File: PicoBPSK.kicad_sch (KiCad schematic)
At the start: 0 parts

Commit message: update sheet settings
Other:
- company: (none) -> okdwtr
- title: (none) -> PicoBPSK
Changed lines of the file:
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@@
 	(generator_version "10.0")
 	(paper "A4")
+	(title_block
+		(title "PicoBPSK")
+		(date "2026-09-03")
+		(rev "0.01")
+		(company "okdwtr")
+		(comment 1 "USB-BPSK Converter Using RP2354")
+	)
 	(sheet_instances
 		(path "/"

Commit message: update sch
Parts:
- added J1: USB_C_Receptacle_USB2.0_16P, symbol Connector:USB_C_Receptacle_USB2.0_16P
- added R1, R2, R3: R, symbol Device:R
- added U1: RP2354A, Package_DFN_QFN:QFN-60-1EP_7x7mm_P0.4mm_EP3.4x3.4mm, symbol MCU_RaspberryPi:RP2354A
- added U2: AMS1117-3.3, Package_TO_SOT_SMD:SOT-223-3_TabPin2, symbol Regulator_Linear:AMS1117-3.3
- added U3: TLV70012_SOT23-5, Package_TO_SOT_SMD:SOT-23-5, symbol Regulator_Linear:TLV70012_SOT23-5
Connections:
- new net: J1.SH (SHIELD), R1.1
- new net: U1.1 (IOVDD), U1.11 (IOVDD), U1.20 (IOVDD), U1.30 (IOVDD), U1.38 (IOVDD), U1.45 (IOVDD)
- new net: U1.23 (DVDD), U1.39 (DVDD), U1.6 (DVDD)
- new net +3V3: U2.2 (VO), U3.1 (IN), U3.3 (EN)
- new net D+: J1.A6 (D+), J1.B6 (D+)
- new net D-: J1.A7 (D-), J1.B7 (D-)
- new net GND: J1.A1 (GND), J1.A12 (GND), J1.B1 (GND), J1.B12 (GND), R1.2, U2.1 (GND), U3.2 (GND)
- new net VBUS: J1.A4 (VBUS), J1.A9 (VBUS), J1.B4 (VBUS), J1.B9 (VBUS)

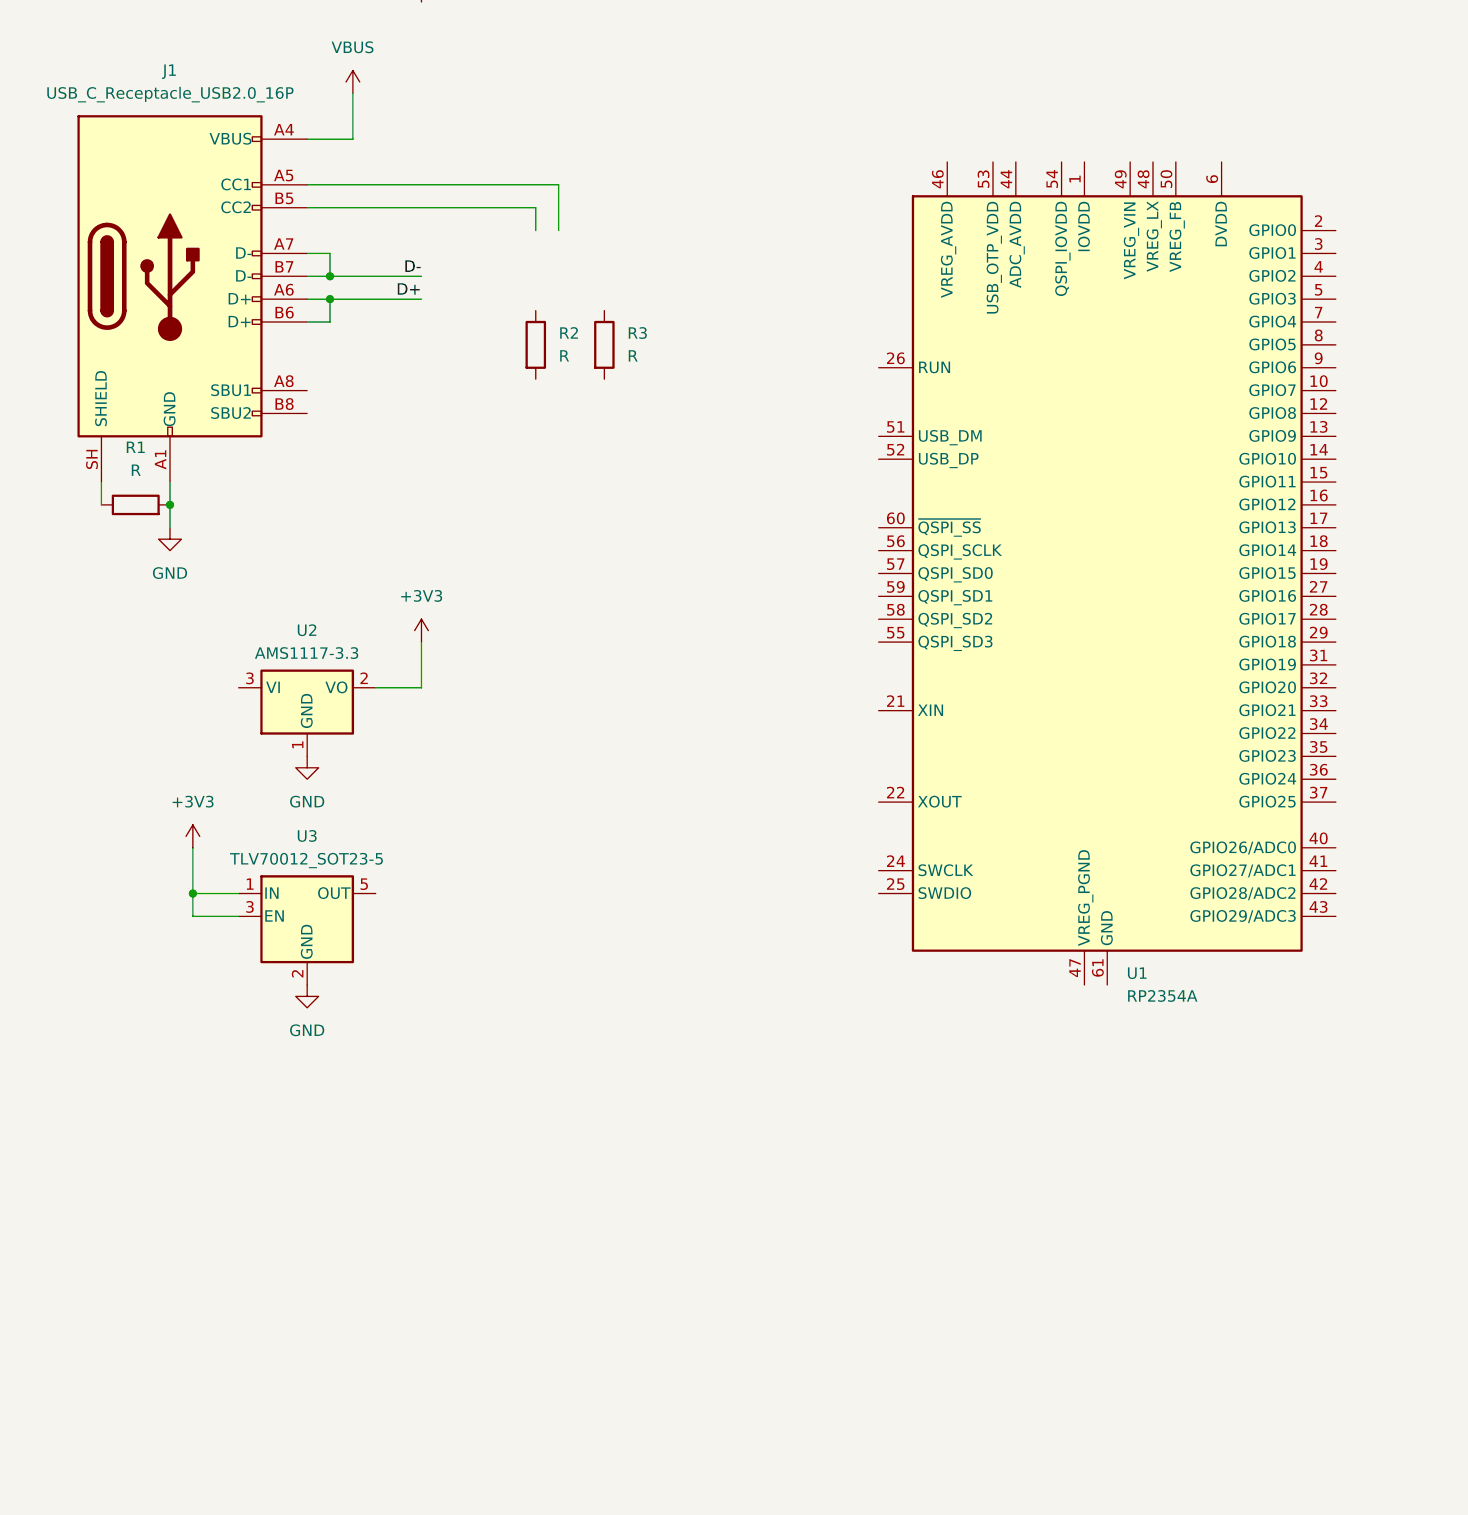
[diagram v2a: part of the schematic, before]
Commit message: update power sch
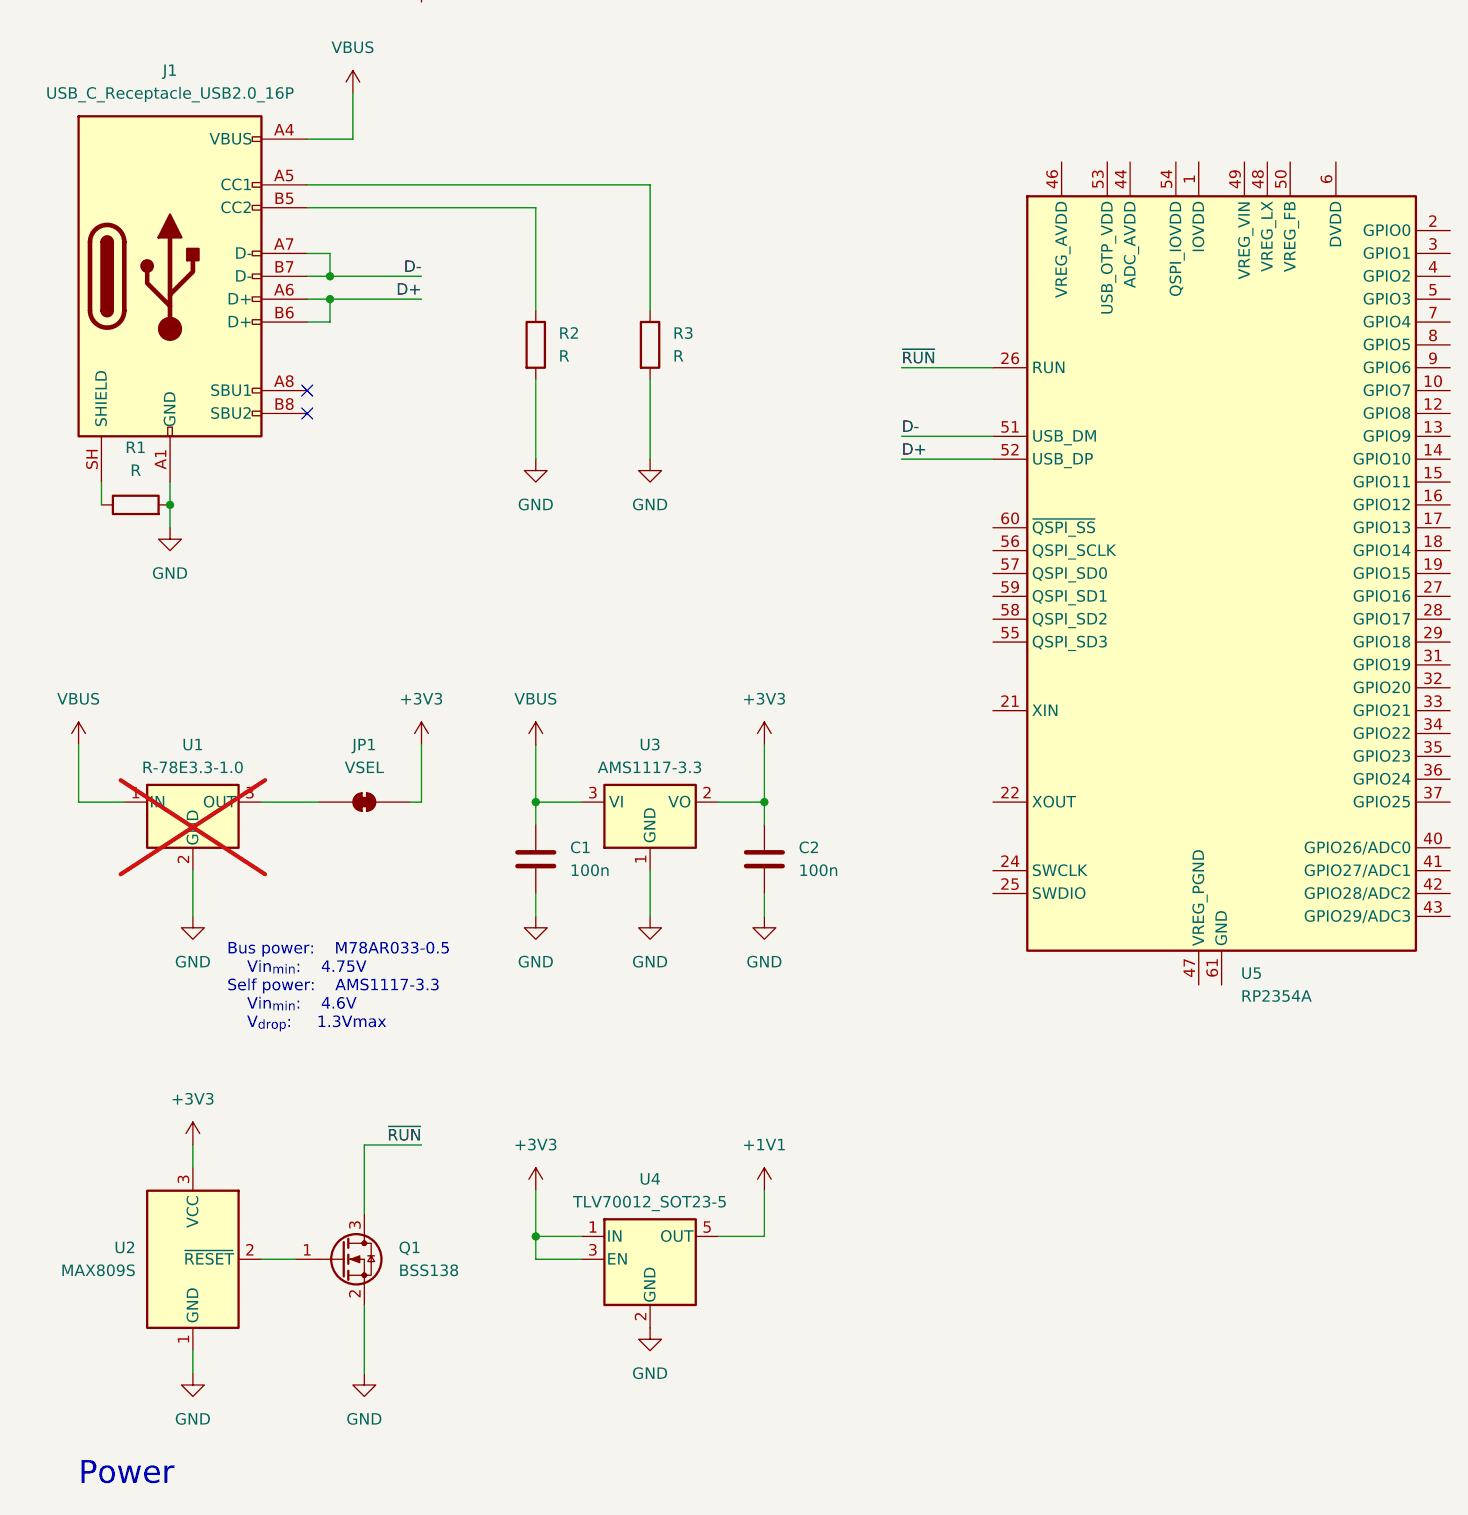
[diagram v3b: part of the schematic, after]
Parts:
- removed U2: AMS1117-3.3, Package_TO_SOT_SMD:SOT-223-3_TabPin2, symbol Regulator_Linear:AMS1117-3.3
- added C1, C2: 100n, Capacitor_SMD:C_0402_1005Metric, symbol Device:C
- added JP1: VSEL, Jumper:SolderJumper-2_P1.3mm_Open_RoundedPad1.0x1.5mm, symbol Jumper:SolderJumper_2_Bridged
- added Q1: BSS138, Package_TO_SOT_SMD:SOT-23, symbol Transistor_FET:BSS138
- added U1: R-78E3.3-1.0, Converter_DCDC:Converter_DCDC_RECOM_R-78E-0.5_THT, symbol Converter_DCDC:R-78E3.3-1.0
- added U2: MAX809S, Package_TO_SOT_SMD:SOT-23, symbol Power_Supervisor:LM809
- added U3: AMS1117-3.3, Package_TO_SOT_SMD:SOT-223-3_TabPin2, symbol Regulator_Linear:AMS1117-3.3
- J1: footprint (none) -> Connector_USB:USB_C_Receptacle_GCT_USB4105-xx-A_16P_TopMnt_Horizontal; LCSC (none) -> C5184243; akizuki (none) -> 114356
- renumbered U3 to U4, U1 to U5
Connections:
- net +3V3: now also C2.1, JP1.2 (B), U2.3 (VCC), U3.2 (VO)
- net D+: now also U5.52 (USB_DP)
- net D-: now also U5.51 (USB_DM)
- net GND: now also R2.2, R3.2, C1.2, C2.2, Q1.2 (S), U1.2 (GND), U2.1 (GND), U3.1 (GND)
- net VBUS: now also C1.1, U1.1 (IN), U3.3 (VI)
- net +1V1: now reaches U4.5 (OUT)
- net at R3.1: now also J1.A5 (CC1)
- net at R2.1: now also J1.B5 (CC2)
- net ~{RUN}: now reaches U5.26 (RUN)
- net ~{RUN}: now also Q1.3 (D)
- new net: JP1.1 (A), U1.3 (OUT)
- new net: Q1.1 (G), U2.2 (~{RESET})
- no-connect marks 0 -> 2
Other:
- note added: "Bus power: M78AR033-0.5 Vin_{min}: 4.75V Self power: AMS1117-3.3 Vin_{min}: 4.6V V_{drop}: 1.3Vmax"
- note added: "Power"
- moved on the sheet: R3, U4, U5

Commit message: update rp2354
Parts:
- added C3, C7, C9: 100n, Capacitor_SMD:C_0402_1005Metric, symbol Device:C
- added R4, R6, R7: 1k, Resistor_SMD:R_0603_1608Metric, symbol Device:R
- added SW2: RUN, Button_Switch_SMD:SW_Push_SPST_NO_Alps_SKRK, symbol Switch:SW_Push
- added SW3: BOOTSEL, Button_Switch_SMD:SW_Push_SPST_NO_Alps_SKRK, symbol Switch:SW_Push
- added SW4: IO3, Button_Switch_SMD:SW_Push_SPST_NO_Alps_SKRK, symbol Switch:SW_Push
- U5: LCSC (none) -> C41378174; akizuki (none) -> 131439
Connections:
- net +1V1: now also U5.23 (DVDD), U5.39 (DVDD), U5.6 (DVDD)
- net +3V3: now also U5.1 (IOVDD), U5.11 (IOVDD), U5.20 (IOVDD), U5.30 (IOVDD), U5.38 (IOVDD), U5.45 (IOVDD), U5.46 (VREG_AVDD), U5.49 (VREG_VIN), U5.53 (USB_OTP_VDD), U5.54 (QSPI_IOVDD), C9.1, SW4.1
- net GND: now also U5.47 (VREG_PGND), U5.61 (GND), C3.2, C7.2, R7.1, SW2.1, SW3.1
- new net: C3.1, R4.1, SW2.2
- new net: C7.1, R6.1, SW3.2
- new net IO3: C9.2, R7.2, SW4.2
- new net RUN: R4.2
- new net ~{QSPI_SS}: R6.2
- no-connect marks 2 -> 4
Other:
- note added: "Input - Switch"

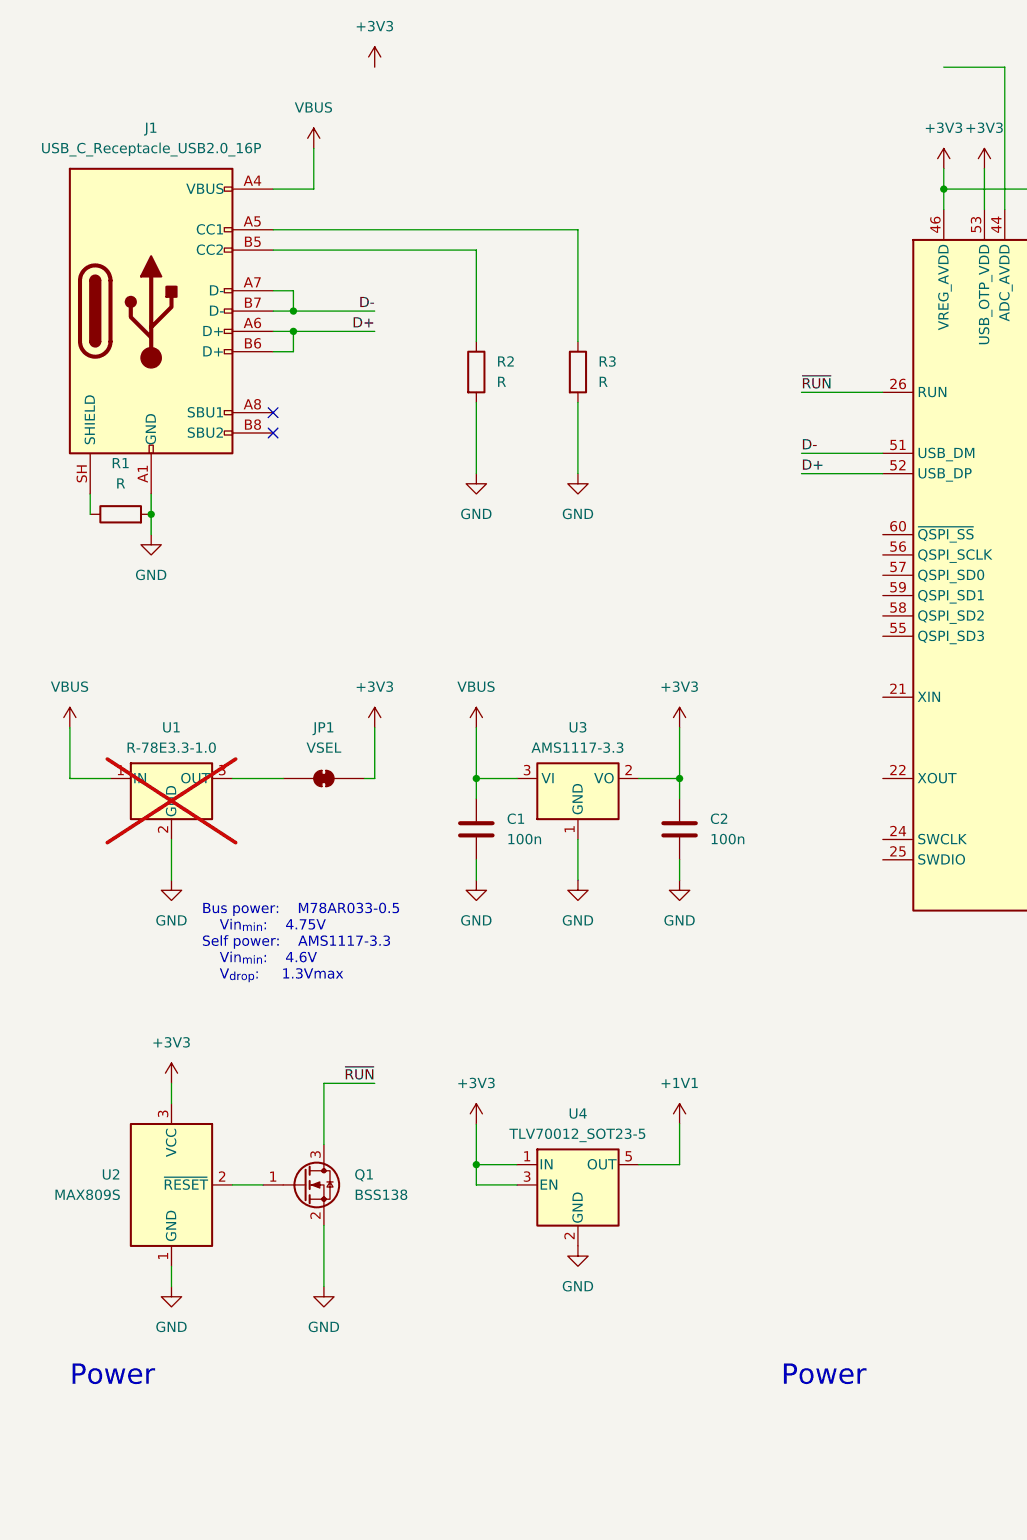
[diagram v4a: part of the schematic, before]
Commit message: move usb power to other sheet
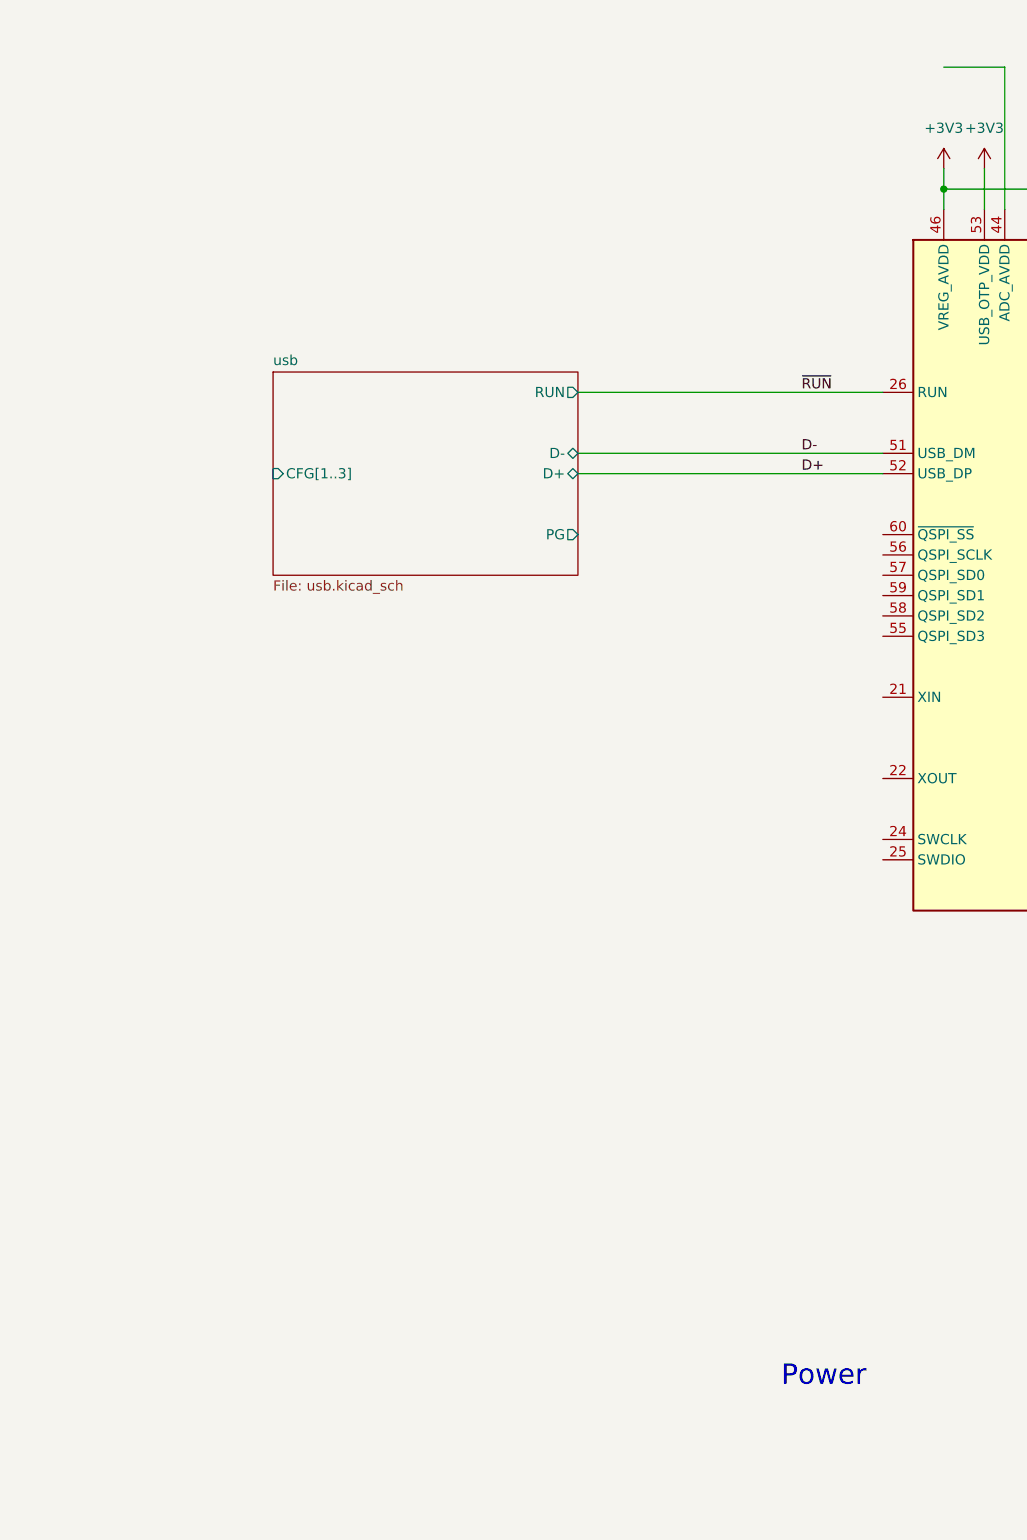
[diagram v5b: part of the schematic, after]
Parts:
- removed C1, C2: 100n, Capacitor_SMD:C_0402_1005Metric, symbol Device:C
- removed J1: USB_C_Receptacle_USB2.0_16P, Connector_USB:USB_C_Receptacle_GCT_USB4105-xx-A_16P_TopMnt_Horizontal, symbol Connector:USB_C_Receptacle_USB2.0_16P
- removed JP1: VSEL, Jumper:SolderJumper-2_P1.3mm_Open_RoundedPad1.0x1.5mm, symbol Jumper:SolderJumper_2_Bridged
- removed Q1: BSS138, Package_TO_SOT_SMD:SOT-23, symbol Transistor_FET:BSS138
- removed R1, R2, R3: R, symbol Device:R
- removed U1: R-78E3.3-1.0, Converter_DCDC:Converter_DCDC_RECOM_R-78E-0.5_THT, symbol Converter_DCDC:R-78E3.3-1.0
- removed U2: MAX809S, Package_TO_SOT_SMD:SOT-23, symbol Power_Supervisor:LM809
- removed U3: AMS1117-3.3, Package_TO_SOT_SMD:SOT-223-3_TabPin2, symbol Regulator_Linear:AMS1117-3.3
- removed U4: TLV70012_SOT23-5, Package_TO_SOT_SMD:SOT-23-5, symbol Regulator_Linear:TLV70012_SOT23-5
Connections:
- no-connect marks 4 -> 2
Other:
- added sheet usb (usb.kicad_sch)
- note removed: "Bus power: M78AR033-0.5 Vin_{min}: 4.75V Self power: AMS1117-3.3 Vin_{min}: 4.6V V_{drop}: 1.3Vmax"

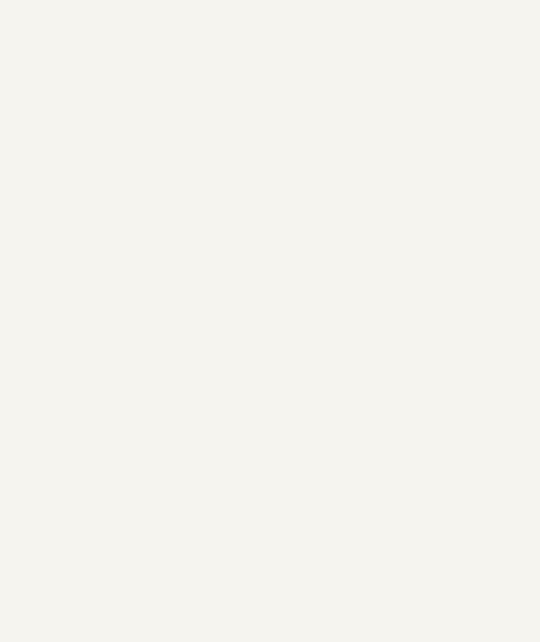
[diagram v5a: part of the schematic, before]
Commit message: add hole
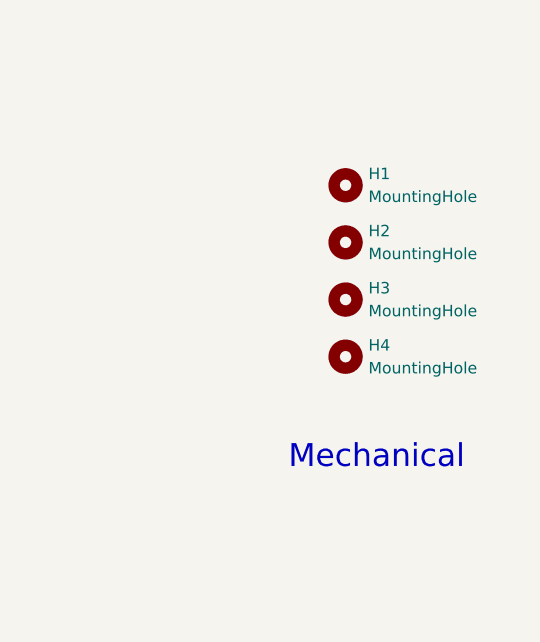
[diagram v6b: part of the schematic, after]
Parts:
- added H1, H2, H3, H4: MountingHole, MountingHole:MountingHole_3.2mm_M3, symbol Mechanical:MountingHole
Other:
- note added: "Mechanical"

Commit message: update sch
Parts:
- added C15, C16, C17, C20, C21, C23, C24, C25, C26, C27, C28: 100n, Capacitor_SMD:C_0402_1005Metric, symbol Device:C
- added R8, R9: 22, Resistor_SMD:R_0603_1608Metric, symbol Device:R
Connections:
- net +1V1: now also C15.1, C16.1, C17.1
- net +3V3: now also C20.1, C21.1, C23.1, C24.1, C25.1, C26.1, C27.1, C28.1
- net D+: now also R8.2
- net D-: now also R9.2
- net GND: now also C15.2, C16.2, C17.2, C20.2, C21.2, C23.2, C24.2, C25.2, C26.2, C27.2, C28.2
- new net usb/D+: R8.1
- new net usb/D-: R9.1
- no-connect marks 2 -> 3
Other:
- note removed: "Power"
- moved on the sheet: C3, C7, C9, R4, R6, R7, SW2, SW3, SW4
